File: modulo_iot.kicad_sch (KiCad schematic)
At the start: 38 parts, among them J2 SMA_CONNECTOR, Q2 BC817, Q3 BC817, Q4 BC817, Q5 BC817, Q6 BC817, Q7 BC817, U5 BG95-M3

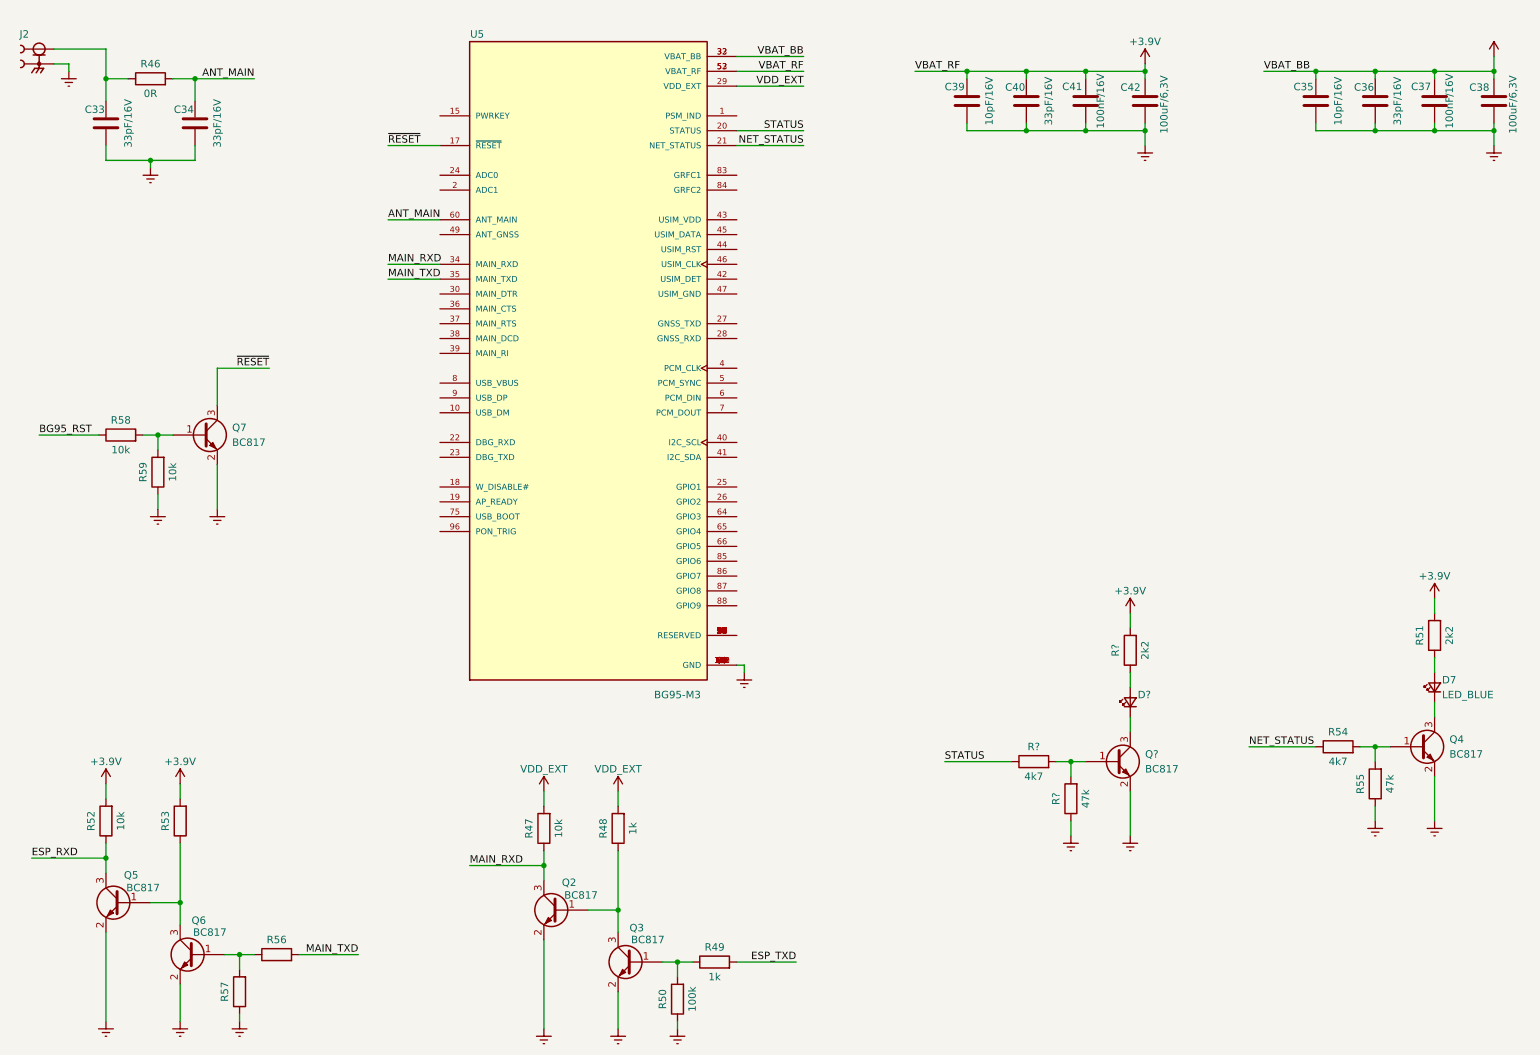
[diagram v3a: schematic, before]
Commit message: Adicionado regulador 3.3V
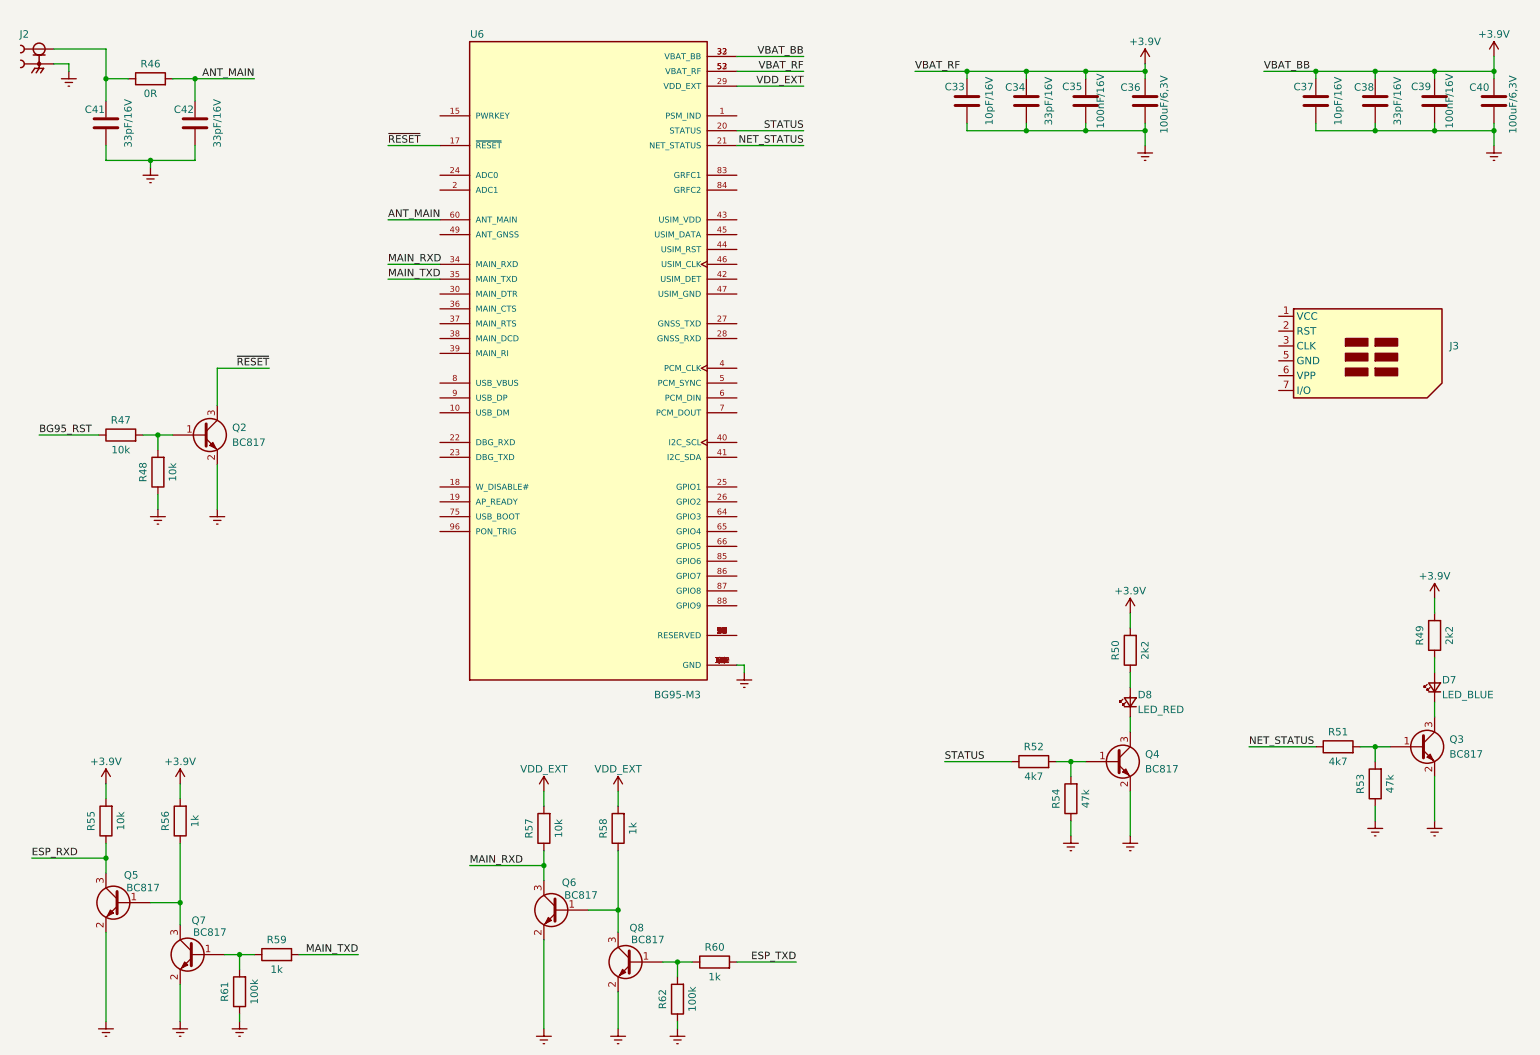
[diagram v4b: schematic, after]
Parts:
- added J3: (no value), symbol Connector:SIM_Card
- D8: renamed from D?; value (none) -> LED_RED; footprint (none) -> LED_SMD:LED_0603_1608Metric_Pad1.05x0.95mm_HandSolder
- R56: renamed from R53; value (none) -> 1k; footprint (none) -> Resistor_SMD:R_0402_1005Metric_Pad0.72x0.64mm_HandSolder
- R59: renamed from R56; value (none) -> 1k
- R61: renamed from R57; value (none) -> 100k
- gave numbers to parts that had none: 4
- renumbered C39 to C33, C40 to C34, C41 to C35, C42 to C36, C35 to C37, C36 to C38, C37 to C39, C38 to C40, C33 to C41, C34 to C42, Q7 to Q2, Q4 to Q3, Q2 to Q6, Q6 to Q7, Q3 to Q8, R58 to R47, R59 to R48, R51 to R49, R54 to R51, R55 to R53, R52 to R55, R47 to R57, R48 to R58, R49 to R60, R50 to R62, U5 to U6

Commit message: Inserido o circuito do SIm Card
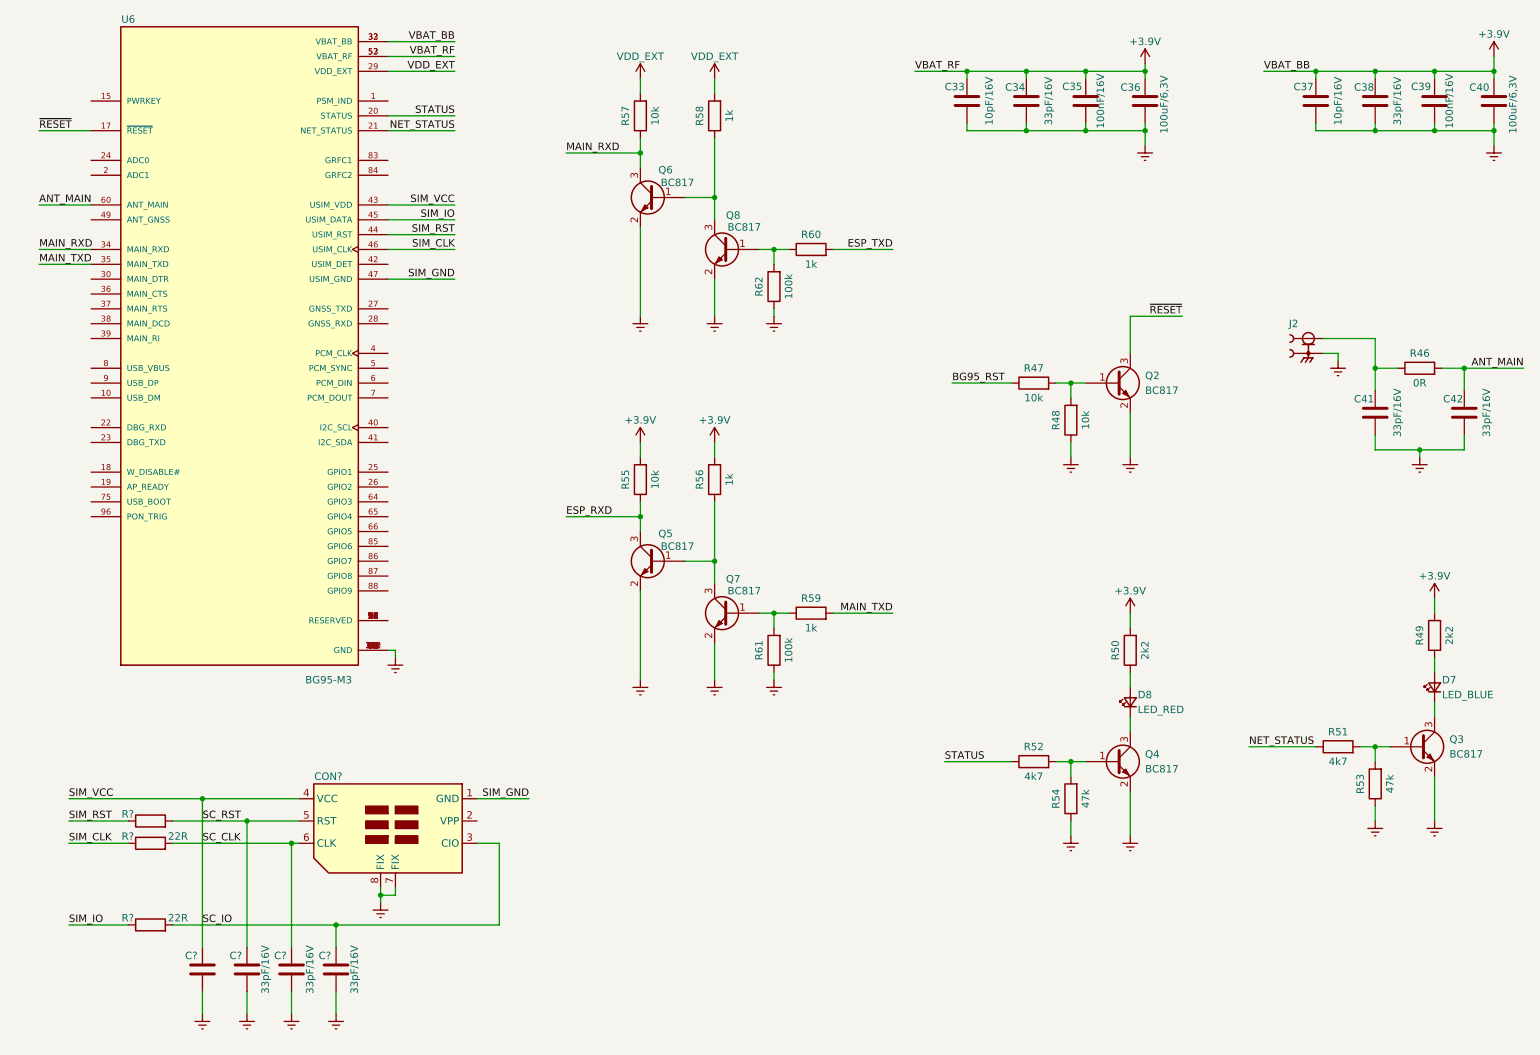
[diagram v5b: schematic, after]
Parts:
- removed J3: (no value), symbol Connector:SIM_Card
- added C? (x3): 33pF/16V, Capacitor_SMD:C_0402_1005Metric_Pad0.74x0.62mm_HandSolder, symbol Device:C
- added C?: (no value), symbol Device:C
- added CON?: (no value), symbol Alexandre_Library:SIM_CARD
- added R?: (no value), Resistor_SMD:R_0402_1005Metric_Pad0.72x0.64mm_HandSolder, symbol Device:R
- added R? (x2): 22R, Resistor_SMD:R_0402_1005Metric_Pad0.72x0.64mm_HandSolder, symbol Device:R
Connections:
- net GNDREF: now also C?.1, C?.1, C?.1, C?.1, CON?.7 (FIX), CON?.8 (FIX)
- net SC_CLK: now reaches U6.43 (USIM_VDD)
- net SC_CLK: now also C?.2, C?.2, C?.2, C?.2, CON?.3 (CIO), CON?.4 (VCC), CON?.5 (RST), CON?.6 (CLK), R?.2, R?.2, R?.2
- net SIM_RST: now reaches U6.44 (USIM_RST)
- net SIM_RST: now also R?.1
- net SIM_IO: now reaches U6.45 (USIM_DATA)
- net SIM_IO: now also R?.1
- net SIM_CLK: now reaches U6.46 (USIM_CLK)
- net SIM_CLK: now also R?.1
- net SIM_GND: now reaches U6.47 (USIM_GND)
- net SIM_GND: now also CON?.1 (GND)
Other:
- moved on the sheet: C41, C42, J2, Q2, Q5, Q6, Q7, Q8, R46, R47, R48, R55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

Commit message: Adicionado hierarchical label
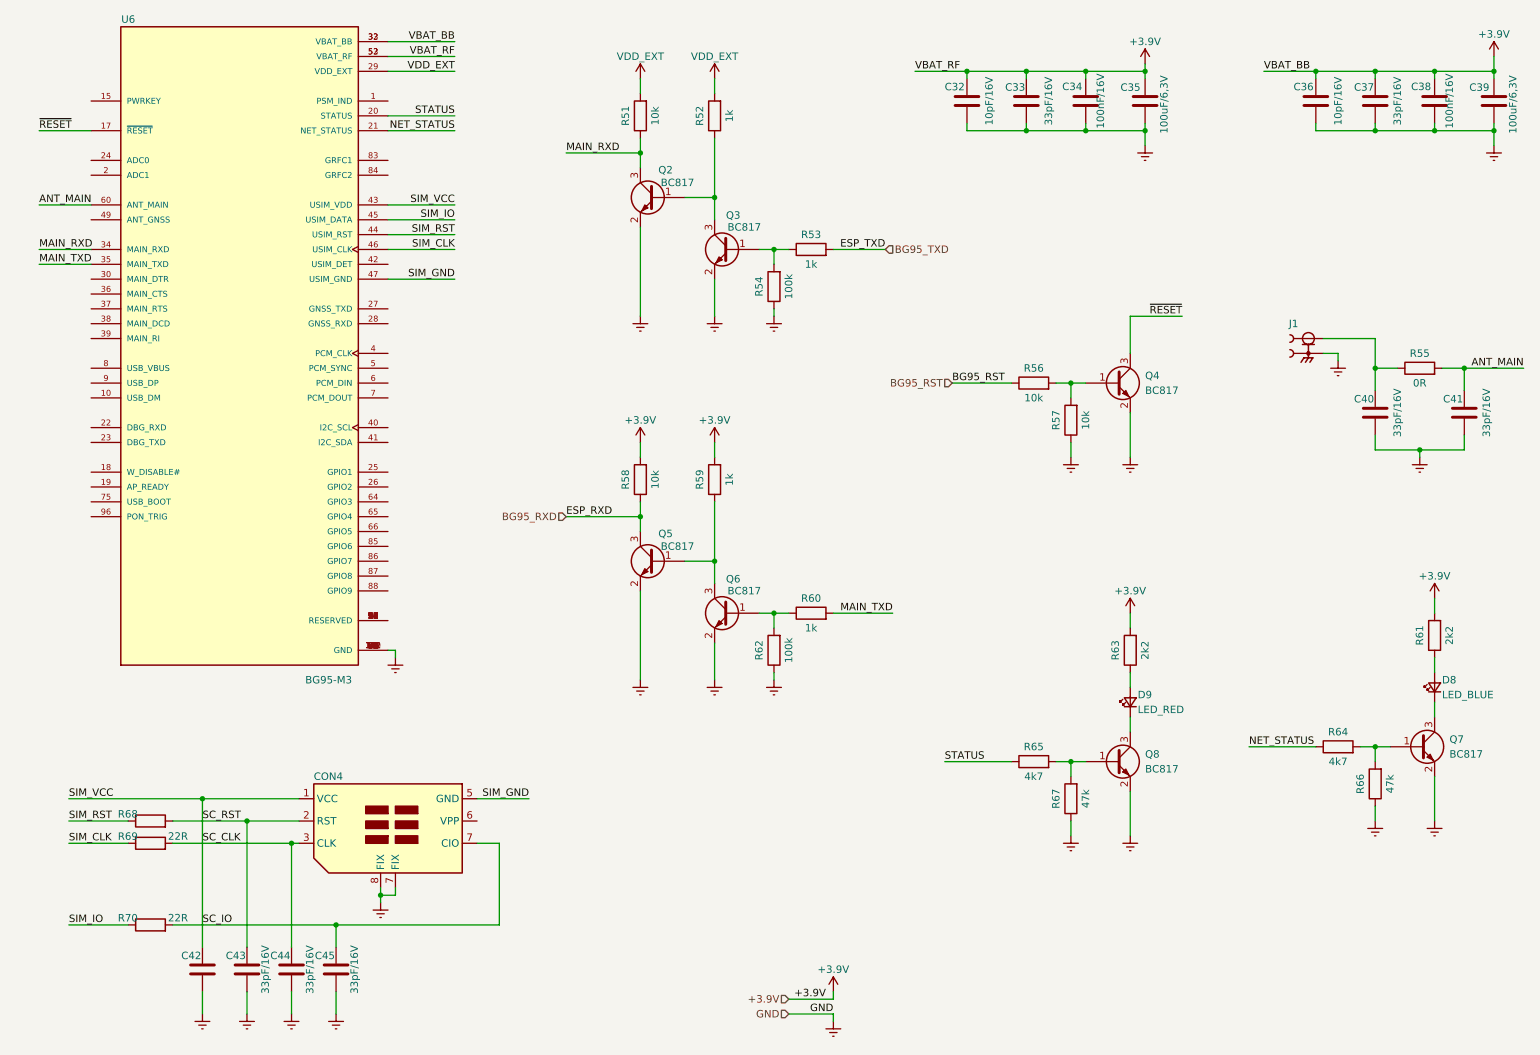
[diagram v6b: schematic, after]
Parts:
- gave numbers to parts that had none: 8
- renumbered C33 to C32, C34 to C33, C35 to C34, C36 to C35, C37 to C36, C38 to C37, C39 to C38, C40 to C39, C41 to C40, C42 to C41, D7 to D8, D8 to D9, J2 to J1, Q6 to Q2, Q8 to Q3, Q2 to Q4, Q7 to Q6, Q3 to Q7, Q4 to Q8, R57 to R51, R58 to R52, R60 to R53, R62 to R54, R46 to R55, R47 to R56, R48 to R57, R55 to R58, R56 to R59, R59 to R60, R49 to R61, R61 to R62, R50 to R63, R51 to R64, R52 to R65, R53 to R66, R54 to R67
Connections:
- net SC_CLK: now also CON4.1 (VCC), CON4.2 (RST), CON4.7 (FIX); no longer CON4.4 (VCC), CON4.5 (RST), CON4.6 (CLK)
- net SIM_GND: now also CON4.5 (GND); no longer CON4.1 (GND)
- net ESP_RXD renamed BG95_RXD
- net ESP_TXD renamed BG95_TXD

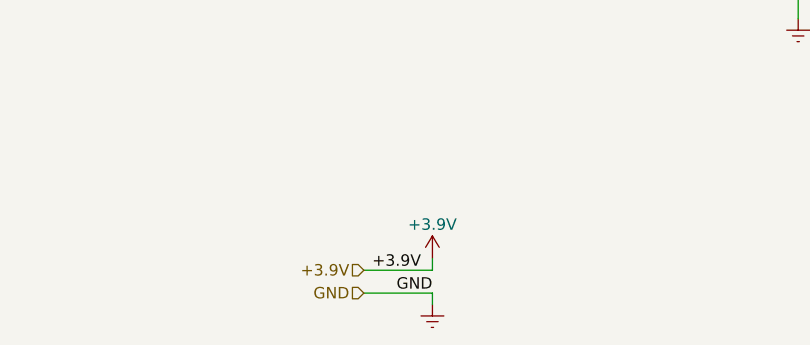
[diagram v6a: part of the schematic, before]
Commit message: Cont. hierarchical label e descrição das folhas
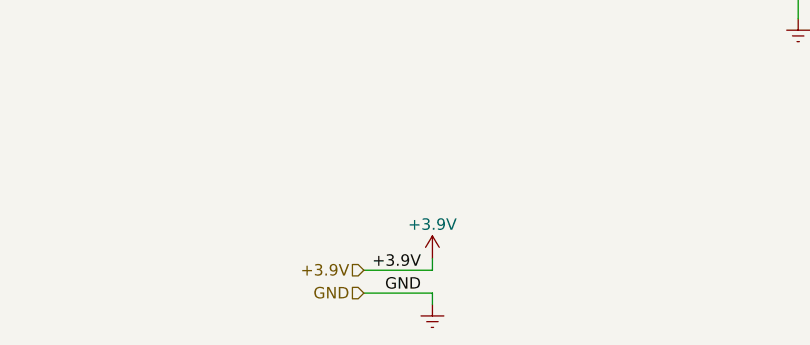
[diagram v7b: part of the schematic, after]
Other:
- company: (none) -> Magalhaes
- title: (none) -> BG95-M3
